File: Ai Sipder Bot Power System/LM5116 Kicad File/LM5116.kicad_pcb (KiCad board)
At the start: 4 copper layers, 60.2 x 83.5 mm, 89 parts, among them J1 XT60-M, J10 PH1-01-UA, J11 PH1-01-UA, J12 PH1-01-UA, J13 PH1-01-UA, J14 61300311121, J15 61300311121, J16 61300311121, J17 61300311121, J18 61300311121, J19 61300311121, J2 PH1-01-UA, J20 61300311121, J21 61300311121, J22 61300311121, J23 61300311121, J24 61300311121, J25 61300311121, J26 691137710002, J3 PH1-01-UA, J4 PH1-01-UA, J5 PH1-01-UA, J6 PH1-01-UA, J7 PH1-01-UA, J8 PH1-01-UA, J9 PH1-01-UA, Q1 CSD17304Q3, Q2 CSD17304Q3, Q3 CSD17304Q3, Q4 CSD17304Q3, Q5 2N7002, Q6 IQDH29NE2LM5CG, U1 LM25116MHX/NOPB, U2 TLV1701AIDBVR, U3 TL431DBZ

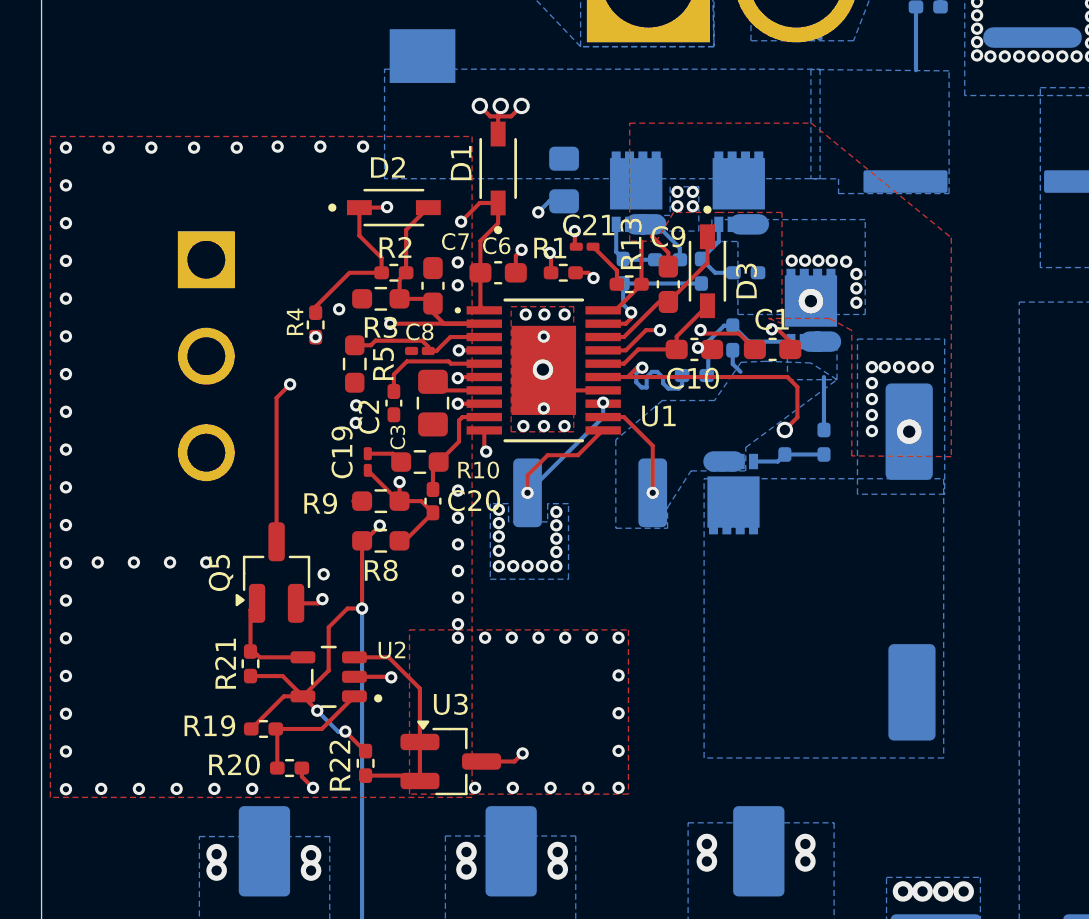
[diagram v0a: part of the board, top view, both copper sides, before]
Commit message: Reduce Vias for AGND ground
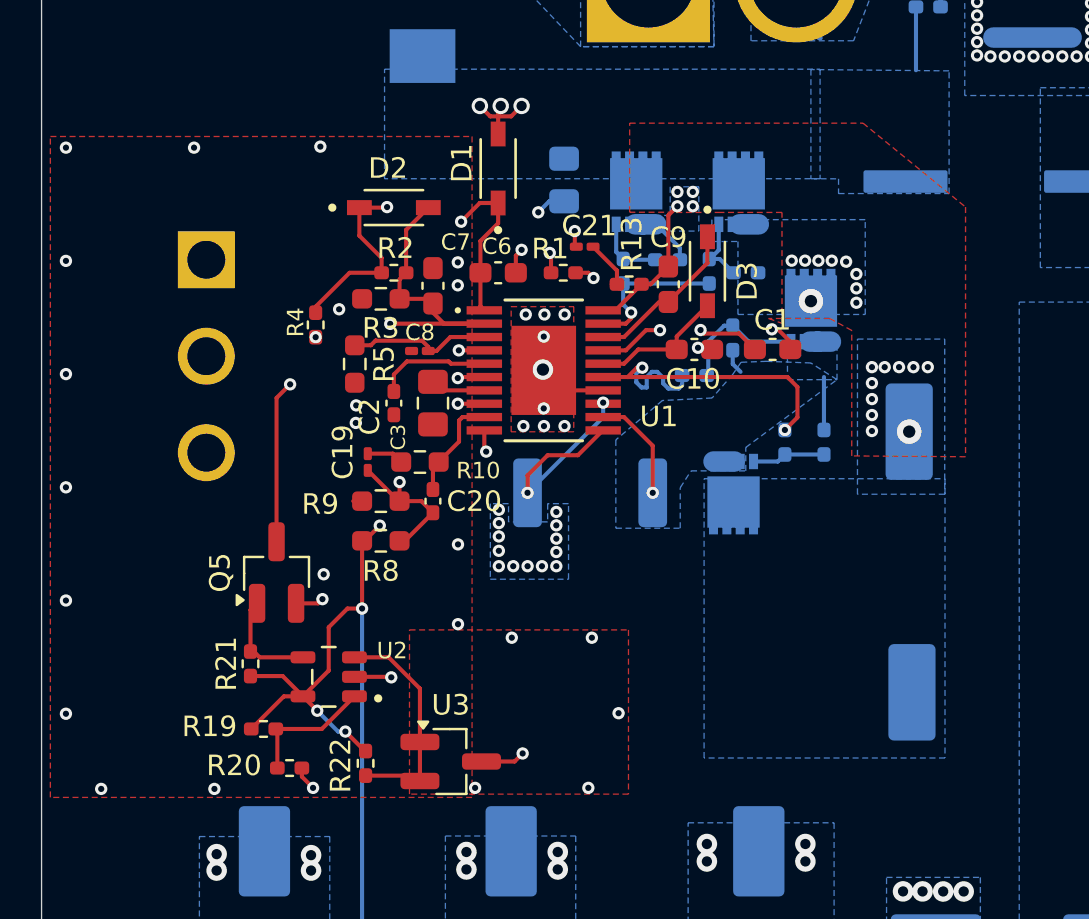
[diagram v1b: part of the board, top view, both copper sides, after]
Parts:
- moved R11 0.38 mm to (145.4, 78.7)
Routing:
- net /SW: track 10.9 -> 11.4 mm
- net Net-(Q1-Gate): track 3.88 -> 3.36 mm
- net GND: vias 70 -> 32

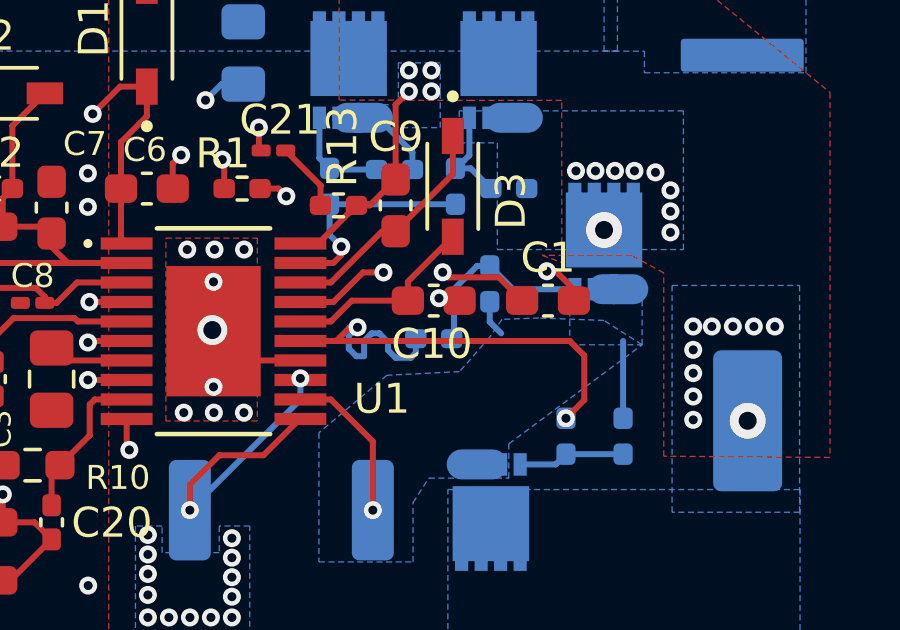
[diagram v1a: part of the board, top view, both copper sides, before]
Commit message: Adjust trace length of LO
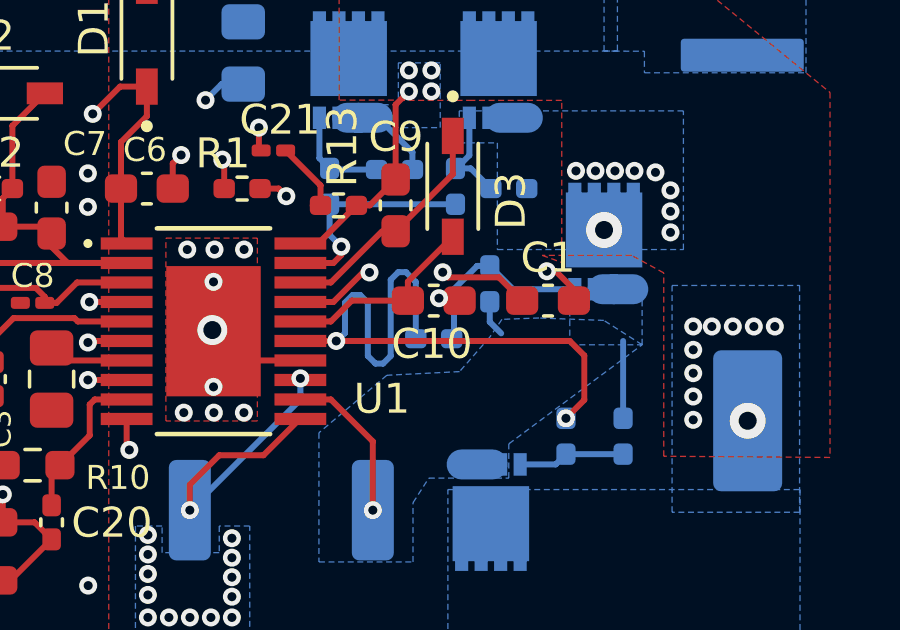
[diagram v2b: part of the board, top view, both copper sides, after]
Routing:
- net /LO: track 17.8 -> 22.7 mm

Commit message: Update Vias
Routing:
- net GND: track 12.2 -> 12.0 mm, vias 32 -> 34
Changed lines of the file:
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@@
-	)
-	(segment
-		(start 128.2965 85.9615)
-		(end 128.1938 86.0642)
-		(width 0.2)
-		(layer "F.Cu")
-		(net "GND")
 	)
 	(segment
@@
 	)
 	(via
+		(at 127.3048 89.8652)
+		(size 0.6)
+		(drill 0.3)
+		(layers "F.Cu" "B.Cu")
+		(remove_unused_layers yes)
+		(keep_end_layers no)
+		(zone_layer_connections "F.Cu" "In1.Cu")
+		(net "GND")
+	)
+	(via
 		(at 126.6282 93.4378)
 		(size 0.6)
@@
 	)
 	(via
-		(at 128.1938 86.0642)
-		(size 0.6)
-		(drill 0.3)
+		(at 129.9464 82.7024)
+		(size 0.6)
+		(drill 0.3)
+		(layers "F.Cu" "B.Cu")
+		(remove_unused_layers yes)
+		(keep_end_layers no)
+		(zone_layer_connections "F.Cu" "In1.Cu")
+		(net "GND")
+	)
+	(via
+		(at 129.286 85.852)
+		(size 0.6)
+		(drill 0.3)
